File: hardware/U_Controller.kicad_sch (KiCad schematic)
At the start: 16 parts, among them J7002 Conn_ARM_JTAG_SWD_10, J7003 USB_C_Receptacle_USB2.0_16P, SW7001 SW_Wuerth_450301014042, U7002 STM32C071RBT6, U7003 USBLC6-2SC6, Y7001 Crystal_GND24

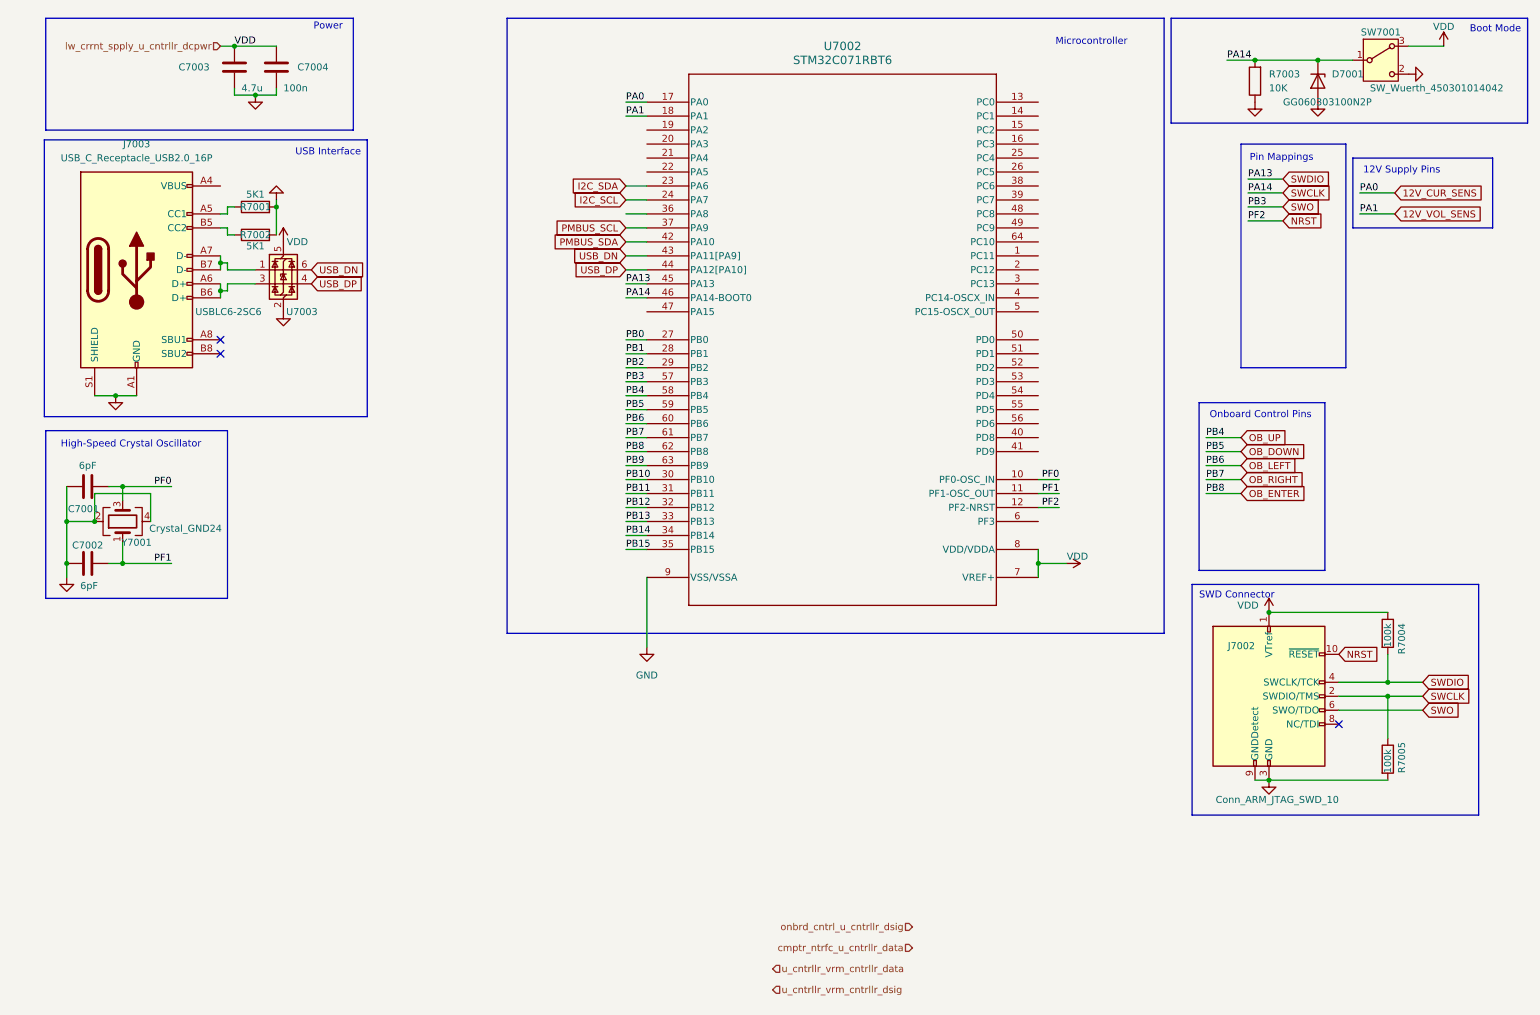
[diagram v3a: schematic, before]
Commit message: feat(schematic): 3.3V global label
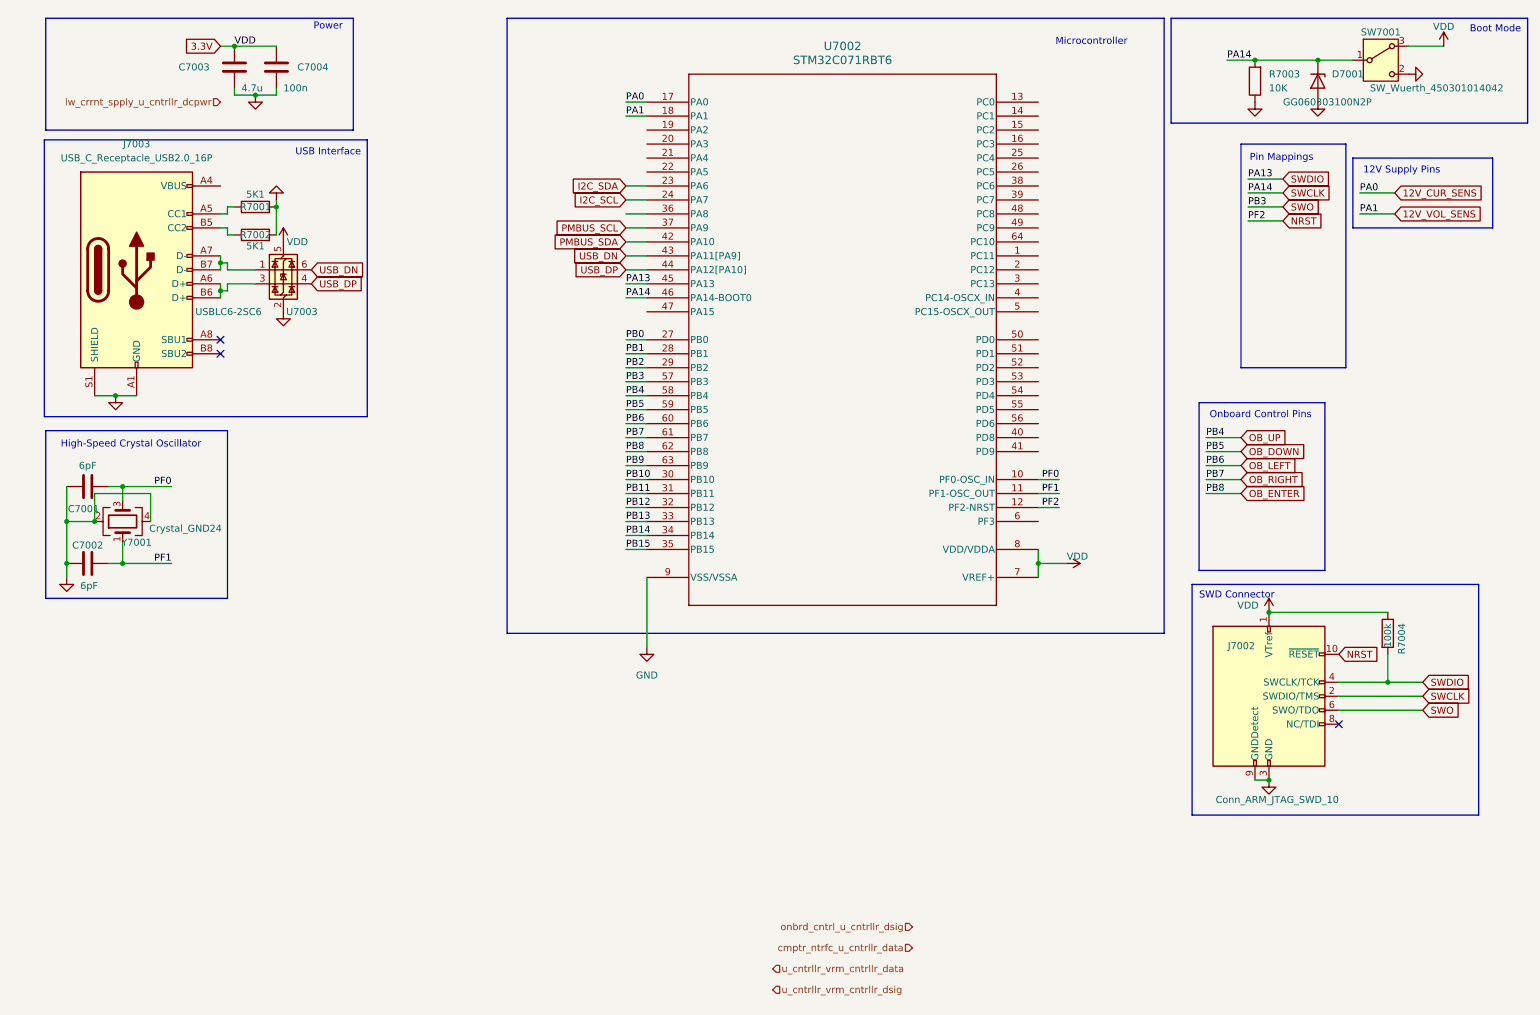
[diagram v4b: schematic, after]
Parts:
- removed R7005: 100k, Resistor_SMD:R_0805_2012Metric, symbol Device:R
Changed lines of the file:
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@@
 	)
 	(junction
-		(at 257.81 137.16)
-		(diameter 0)
-		(color 0 0 0 0)
-	)
-	(junction
 		(at 55.88 48.26)
 		(diameter 0)
@@
 	(wire
 		(pts
-			(xy 248.92 137.16) (xy 257.81 137.16)
-		)
-		(stroke
-			(width 0)
-			(type default)
-		)
-	)
-	(wire
-		(pts
 			(xy 194.31 113.03) (xy 194.31 115.57)
 		)
@@
 	(wire
 		(pts
-			(xy 257.81 137.16) (xy 257.81 144.78)
-		)
-		(stroke
-			(width 0)
-			(type default)
-		)
-	)
-	(wire
-		(pts
 			(xy 119.38 100.33) (xy 123.19 100.33)
 		)
@@
 	(wire
 		(pts
-			(xy 236.22 152.4) (xy 257.81 152.4)
-		)
-		(stroke
-			(width 0)
-			(type default)
-		)
-	)
-	(wire
-		(pts
 			(xy 224.79 100.33) (xy 231.14 100.33)
 		)
@@
 	(wire
 		(pts
-			(xy 257.81 137.16) (xy 264.16 137.16)
+			(xy 248.92 137.16) (xy 264.16 137.16)
 		)
 		(stroke
@@
 		)
 	)
+	(global_label "3.3V"
+		(shape input)
+		(at 45.72 19.05 180)
+		(fields_autoplaced yes)
+		(effects
+			(font
+				(size 1.27 1.27)
+			)
+			(justify right)
+		)
+		(property "Intersheetrefs" "${INTERSHEET_REFS}"
+			(at 38.6224 19.05 0)
+			(effects
+				(font
+					(size 1.27 1.27)
+				)
+				(justify right)
+				(hide yes)
+			)
+		)
+	)
 	(global_label "USB_DN"
 		(shape input)
@@
 	(hierarchical_label "lw_crrnt_spply_u_cntrllr_dcpwr"
 		(shape input)
-		(at 45.72 19.05 180)
+		(at 45.72 29.21 180)
 		(fields_autoplaced yes)
 		(effects
@@
 					(unit 1)
 				)
-			)
-		)
-	)
-	(symbol
-		(lib_id "Device:R")
-		(at 257.81 148.59 0)
-		(unit 1)
-		(exclude_from_sim no)
-		(in_bom yes)
-		(on_board yes)
-		(dnp no)
-		(property "Reference" "R7005"
-			(at 260.35 151.13 90)
-			(effects
-				(font
-					(size 1.27 1.27)
-				)
-				(justify left)
-			)
-		)
-		(property "Value" "100k"
-			(at 257.81 151.13 90)
-			(effects
-				(font
-					(size 1.27 1.27)
-				)
-				(justify left)
-			)
-		)
-		(property "Footprint" "Resistor_SMD:R_0805_2012Metric"
-			(at 256.032 148.59 90)
-			(effects
-				(font
-					(size 1.27 1.27)
-				)
-				(hide yes)
-			)
-		)
-		(property "Datasheet" "~"
-			(at 257.81 148.59 0)
-			(effects
-				(font
-					(size 1.27 1.27)
-				)
-				(hide yes)
-			)
-		)
-		(property "Description" "Resistor"
-			(at 257.81 148.59 0)
-			(effects
-				(font
-					(size 1.27 1.27)
-				)
-				(hide yes)
-			)
-		)
-		(pin "1"
-		)
-		(pin "2"
-		)
-		(instances
-			(project "gpu-external-power-supply"
-				(path "/d5303413-7068-41ba-88e3-39dfa38d31b7/027ff087-ab1d-45e5-9d8f-c94102656fe5"
-					(reference "R7005")
-					(unit 1)
-				)

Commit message: chore(schematic): add global pins
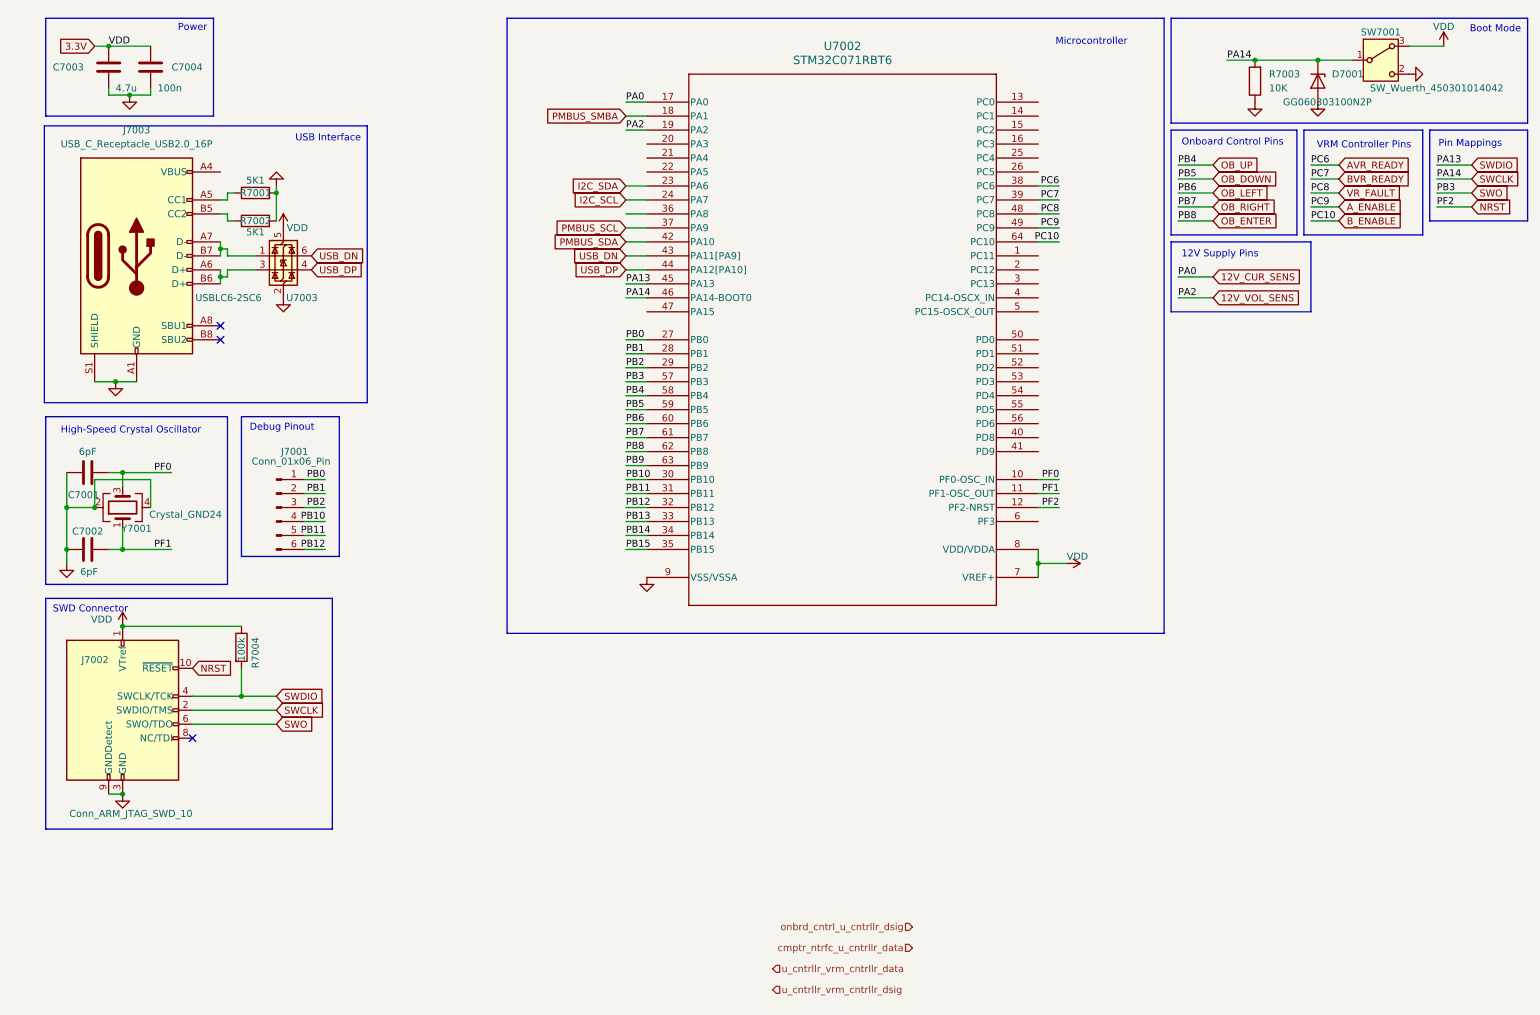
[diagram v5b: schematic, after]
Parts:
- added J7001: Conn_01x06_Pin, symbol Connector:Conn_01x06_Pin
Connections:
- net 12V_VOL_SENS: now also U7002.19 (PA2); no longer U7002.18 (PA1)
- net PB0: now also J7001.1 (Pin_1)
- net PB1: now also J7001.2 (Pin_2)
- net PB10: now also J7001.4 (Pin_4)
- net PB11: now also J7001.5 (Pin_5)
- net PB12: now also J7001.6 (Pin_6)
- net PB2: now also J7001.3 (Pin_3)
- net AVR_READY: now reaches U7002.38 (PC6)
- net BVR_READY: now reaches U7002.39 (PC7)
- net VR_FAULT: now reaches U7002.48 (PC8)
- net A_ENABLE: now reaches U7002.49 (PC9)
- net B_ENABLE: now reaches U7002.64 (PC10)
- new net PMBUS_SMBA: U7002.18 (PA1)
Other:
- note added: "Debug Pinout"
- note added: "VRM Controller Pins"
- moved on the sheet: C7001, C7002, C7003, C7004, J7002, J7003, R7001, R7002, R7004, U7003, Y7001

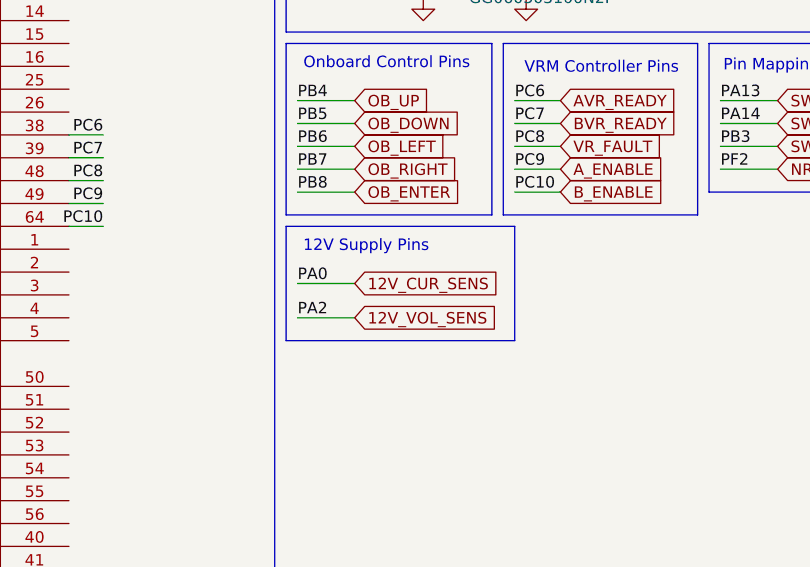
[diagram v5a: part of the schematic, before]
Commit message: fix(schematic): Minor Style changes to u controller and onboard control
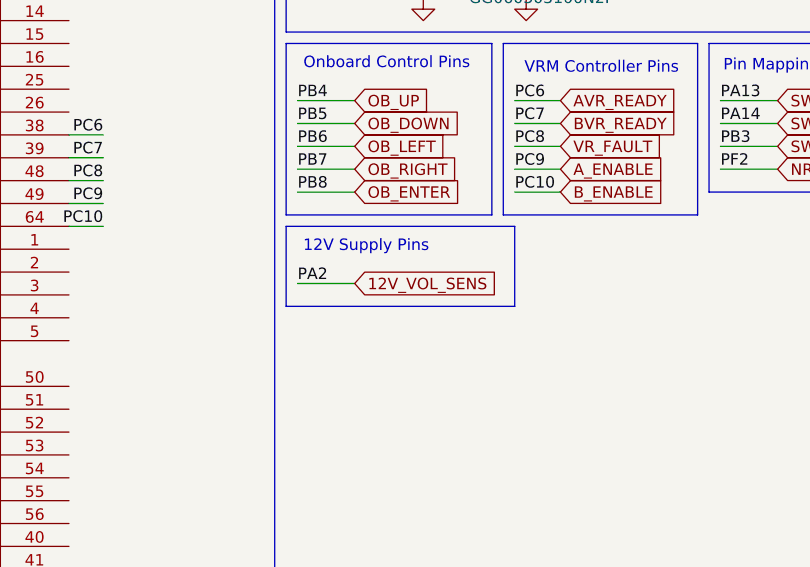
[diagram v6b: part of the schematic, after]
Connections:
- net 12V_CUR_SENS renamed PA0
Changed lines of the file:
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@@
 	(wire
 		(pts
-			(xy 219.71 64.77) (xy 226.06 64.77)
+			(xy 219.71 60.96) (xy 226.06 60.96)
 		)
 		(stroke
@@
 		(pts
 			(xy 60.96 105.41) (xy 64.77 105.41)
-		)
-		(stroke
-			(width 0)
-			(type default)
-		)
-	)
-	(wire
-		(pts
-			(xy 219.71 60.96) (xy 226.06 60.96)
 		)
 		(stroke
@@
 	(rectangle
 		(start 218.44 54.61)
-		(end 243.84 67.31)
+		(end 243.84 63.5)
 		(stroke
 			(width 0)
@@
 	)
 	(label "PA2"
-		(at 219.71 64.77 0)
+		(at 219.71 60.96 0)
 		(fields_autoplaced yes)
 		(effects
@@
 	(label "PB5"
 		(at 119.38 85.09 0)
-		(fields_autoplaced yes)
-		(effects
-			(font
-				(size 1.27 1.27)
-			)
-			(justify left bottom)
-		)
-	)
-	(label "PA0"
-		(at 219.71 60.96 0)
 		(fields_autoplaced yes)
 		(effects
@@
 	(global_label "12V_VOL_SENS"
 		(shape input)
-		(at 226.06 64.77 0)
+		(at 226.06 60.96 0)
 		(fields_autoplaced yes)
 		(effects
@@
 		)
 		(property "Intersheetrefs" "${INTERSHEET_REFS}"
-			(at 242.8337 64.77 0)
+			(at 242.8337 60.96 0)
 			(effects
 				(font
-					(size 1.27 1.27)
-				)
-				(justify left)
-				(hide yes)
-			)
-		)
-	)
-	(global_label "12V_CUR_SENS"
-		(shape input)
-		(at 226.06 60.96 0)
-		(fields_autoplaced yes)
-		(effects
-			(font
-				(size 1.27 1.27)
-			)
-			(justify left)
-		)
-		(property "Intersheetrefs" "${INTERSHEET_REFS}"
-			(at 243.257 60.96 0)
-			(effects
-				(font

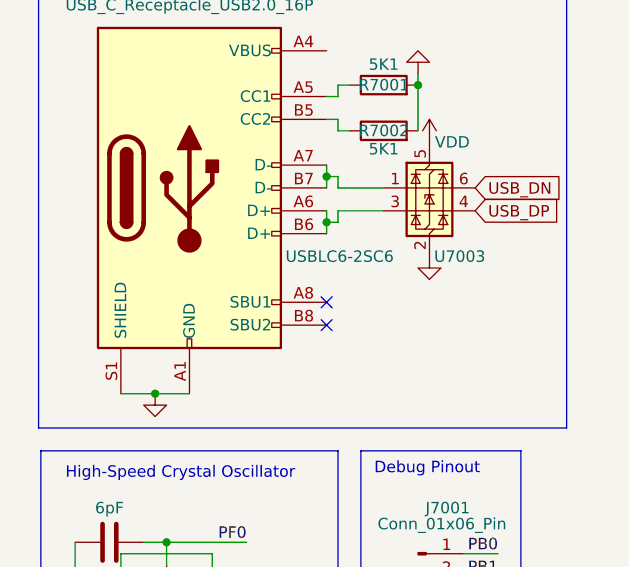
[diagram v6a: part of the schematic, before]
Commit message: feat(PCB): fix all DRC errors
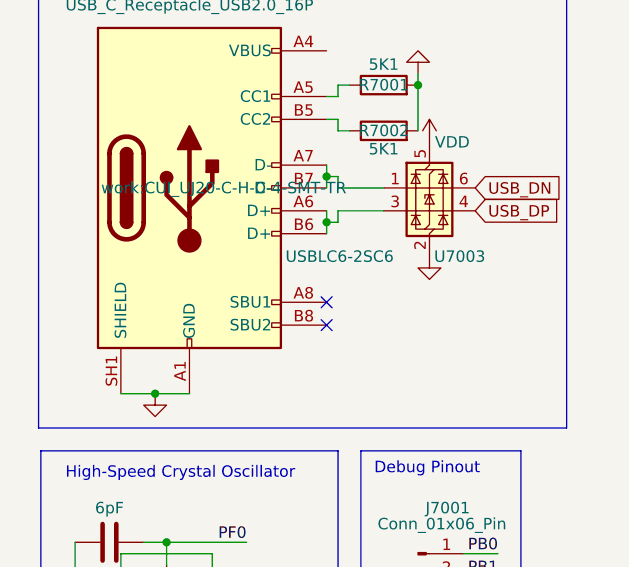
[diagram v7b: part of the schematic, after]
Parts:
- J7003: footprint work:12402012E212A_AMP -> work:CUI_UJ20-C-H-C-4-SMT-TR
- U7002: footprint LQFP-64_STM -> work:LQFP-64_STM
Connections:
- net GND: now also J7003.SH1 (SHIELD), J7003.SH2 (SHIELD), J7003.SH3 (SHIELD), J7003.SH4 (SHIELD); no longer J7003.A12 (GND), J7003.B12 (GND), J7003.S1 (SHIELD)
- net at J7003.A4 (VBUS), J7003.B4 (VBUS): no longer J7003.A9 (VBUS), J7003.B9 (VBUS)
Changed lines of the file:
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@@
 			)
 		)
-		(property "Footprint" "work:12402012E212A_AMP"
+		(property "Footprint" "work:CUI_UJ20-C-H-C-4-SMT-TR"
 			(at 34.29 57.15 0)
 			(effects
@@
 					(size 1.27 1.27)
 				)
-				(hide yes)
 			)
 		)
@@
 			)
 		)
-		(pin "A9"
-		)
 		(pin "B8"
 		)
@@
 		(pin "B7"
 		)
-		(pin "A12"
-		)
 		(pin "B5"
 		)
-		(pin "B12"
-		)
 		(pin "B1"
 		)
-		(pin "S1"
+		(pin "SH3"
 		)
 		(pin "A4"
@@
 		(pin "A8"
 		)
-		(pin "B9"
-		)
 		(pin "A1"
 		)
 		(pin "B4"
+		)
+		(pin "SH4"
+		)
+		(pin "SH1"
+		)
+		(pin "SH2"
 		)
 		(instances
@@
 			)
 		)
-		(property "Footprint" "LQFP-64_STM"
+		(property "Footprint" "work:LQFP-64_STM"
 			(at 123.19 29.21 0)
 			(effects
